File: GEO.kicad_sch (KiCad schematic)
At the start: 17 parts, among them J1 Conn_01x02, U1 Op_Amp

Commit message: changed two pin header
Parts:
- A1: footprint ARDUINO_ARDUINO_MEGA_2560_REV3_A000067 -> footprints:ARDUINO_ARDUINO_MEGA_2560_REV3_A000067; symbol main_pcb:Arduino_Mega -> symbols:Arduino_Mega
- C1: footprint KiCad Footprints:CAPC1608X90 -> footprints:CAPC1608X90; symbol main_pcb:C -> symbols:C
- CO1: footprint JST_B5B-XH-A -> footprints:JST_B5B-XH-A; symbol main_pcb:Conn_CO -> symbols:Conn_CO
- Clk1: footprint TE_5-146280-5 -> footprints:TE_5-146280-5; symbol main_pcb:Clock -> symbols:Clock
- H1, H2: footprint MountingHole:MountingHole_2.1mm -> footprints:MountingHole_2.1mm; symbol main_pcb:MountingHole -> symbols:MountingHole
- J1: footprint Connector_PinHeader_2.00mm:PinHeader_1x02_P2.00mm_Vertical -> Connector_PinSocket_2.54mm:PinSocket_1x02_P2.54mm_Vertical; symbol main_pcb:Conn_01x02 -> symbols:Conn_01x02
- LCD1: footprint CON9_SMT-RA_FCC-FPC2 -> footprints:TE_84952-9_1x09-1MP_P1.0mm_Horizontal; symbol main_pcb:Conn_LCD -> symbols:Conn_LCD
- PM1: footprint KiCad Footprints:JST_SM08B-GHS-TB(LF)(SN) -> footprints:JST_SM08B-GHS-TB(LF)(SN); symbol main_pcb:Conn_PM -> symbols:Conn_PM
- R1, R2: footprint Resistor_THT:R_Axial_DIN0309_L9.0mm_D3.2mm_P12.70mm_Horizontal -> footprints:R_Axial_DIN0309_L9.0mm_D3.2mm_P12.70mm_Horizontal; symbol main_pcb:R -> symbols:R
- R3, R4: footprint KiCad Footprints:R0402 -> footprints:R0402; symbol main_pcb:R -> symbols:R; JLC_3DModel (none) -> 026a4a15ab5c4a92ac0e421d6d013717; JLC_3D_Size (none) -> 1 0.5
- SD1: footprint JST_B6B-XH-A(LF)(SN) -> footprints:JST_B6B-XH-A(LF)(SN); symbol main_pcb:Conn_SD -> symbols:Conn_SD
- TEMP1: footprint KiCad Footprints:JST_B4B-XH-A(LF)(SN) -> footprints:JST_B4B-XH-A(LF)(SN); symbol main_pcb:Conn_Temp -> symbols:Conn_Temp
- U1: footprint Package_TO_SOT_SMD:SOT-353_SC-70-5 -> footprints:SOT-353_SC-70-5; symbol main_pcb:Op_Amp -> symbols:Op_Amp
- U2: footprint KiCad Footprints:DFR1015 Buck_Converter -> footprints:DFR1015 Buck_Converter; symbol main_pcb:Buck_Converter -> symbols:Buck_Converter
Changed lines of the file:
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@@
 	)
 	(symbol
-		(lib_id "main_pcb:Conn_PM")
+		(lib_id "symbols:Conn_PM")
 		(at 139.7 160.02 0)
 		(unit 1)
@@
 			)
 		)
-		(property "Footprint" "KiCad Footprints:JST_SM08B-GHS-TB(LF)(SN)"
+		(property "Footprint" "footprints:JST_SM08B-GHS-TB(LF)(SN)"
 			(at 139.7 160.02 0)
 			(effects
@@
 	)
 	(symbol
-		(lib_id "main_pcb:MountingHole")
+		(lib_id "symbols:MountingHole")
 		(at 241.3 30.48 0)
 		(unit 1)
@@
 			)
 		)
-		(property "Footprint" "MountingHole:MountingHole_2.1mm"
+		(property "Footprint" "footprints:MountingHole_2.1mm"
 			(at 241.3 30.48 0)
 			(effects
@@
 	)
 	(symbol
-		(lib_id "main_pcb:Arduino_Mega")
+		(lib_id "symbols:Arduino_Mega")
 		(at 58.42 111.76 0)
 		(unit 1)
@@
 			)
 		)
-		(property "Footprint" "ARDUINO_ARDUINO_MEGA_2560_REV3_A000067"
+		(property "Footprint" "footprints:ARDUINO_ARDUINO_MEGA_2560_REV3_A000067"
 			(at 58.42 111.76 0)
 			(effects
@@
 	)
 	(symbol
-		(lib_id "main_pcb:R")
+		(lib_id "symbols:R")
 		(at 232.41 68.58 180)
 		(unit 1)
@@
 			)
 		)
-		(property "Footprint" "Resistor_THT:R_Axial_DIN0309_L9.0mm_D3.2mm_P12.70mm_Horizontal"
+		(property "Footprint" "footprints:R_Axial_DIN0309_L9.0mm_D3.2mm_P12.70mm_Horizontal"
 			(at 231.394 68.326 90)
 			(effects
@@
 	)
 	(symbol
-		(lib_id "main_pcb:R")
+		(lib_id "symbols:R")
 		(at 213.36 97.79 180)
 		(unit 1)
@@
 			)
 		)
-		(property "Footprint" "KiCad Footprints:R0402"
+		(property "Footprint" "footprints:R0402"
 			(at 212.344 97.536 90)
 			(effects
@@
 		)
 		(property "Description" "Resistor, US symbol"
+			(at 213.36 97.79 0)
+			(effects
+				(font
+					(size 1.27 1.27)
+				)
+				(hide yes)
+			)
+		)
+		(property "JLC_3DModel" "026a4a15ab5c4a92ac0e421d6d013717"
+			(at 213.36 97.79 0)
+			(effects
+				(font
+					(size 1.27 1.27)
+				)
+				(hide yes)
+			)
+		)
+		(property "JLC_3D_Size" "1 0.5"
 			(at 213.36 97.79 0)
 			(effects
@@
 	)
 	(symbol
-		(lib_id "main_pcb:Conn_01x02")
+		(lib_id "symbols:Conn_01x02")
 		(at 260.35 99.06 270)
 		(unit 1)
@@
 			)
 		)
-		(property "Footprint" "Connector_PinHeader_2.00mm:PinHeader_1x02_P2.00mm_Vertical"
+		(property "Footprint" "Connector_PinSocket_2.54mm:PinSocket_1x02_P2.54mm_Vertical"
 			(at 260.35 99.06 0)
 			(effects
@@
 	)
 	(symbol
-		(lib_id "main_pcb:Conn_CO")
+		(lib_id "symbols:Conn_CO")
 		(at 137.16 119.38 0)
 		(unit 1)
@@
 			)
 		)
-		(property "Footprint" "JST_B5B-XH-A"
+		(property "Footprint" "footprints:JST_B5B-XH-A"
 			(at 137.16 119.38 0)
 			(effects
@@
 	)
 	(symbol
-		(lib_id "main_pcb:MountingHole")
+		(lib_id "symbols:MountingHole")
 		(at 241.3 35.56 0)
 		(unit 1)
@@
 			)
 		)
-		(property "Footprint" "MountingHole:MountingHole_2.1mm"
+		(property "Footprint" "footprints:MountingHole_2.1mm"
 			(at 241.3 35.56 0)
 			(effects
@@
 	)
 	(symbol
-		(lib_id "main_pcb:R")
+		(lib_id "symbols:R")
 		(at 213.36 83.82 180)
 		(unit 1)
@@
 			)
 		)
-		(property "Footprint" "KiCad Footprints:R0402"
+		(property "Footprint" "footprints:R0402"
 			(at 212.344 83.566 90)
 			(effects
@@
 		)
 		(property "Description" "Resistor, US symbol"
+			(at 213.36 83.82 0)
+			(effects
+				(font
+					(size 1.27 1.27)
+				)
+				(hide yes)
+			)
+		)
+		(property "JLC_3DModel" "026a4a15ab5c4a92ac0e421d6d013717"
+			(at 213.36 83.82 0)
+			(effects
+				(font
+					(size 1.27 1.27)
+				)
+				(hide yes)
+			)
+		)
+		(property "JLC_3D_Size" "1 0.5"
 			(at 213.36 83.82 0)
 			(effects
@@
 	)
 	(symbol
-		(lib_id "main_pcb:R")
+		(lib_id "symbols:R")
 		(at 232.41 54.61 180)
 		(unit 1)
@@
 			)
 		)
-		(property "Footprint" "Resistor_THT:R_Axial_DIN0309_L9.0mm_D3.2mm_P12.70mm_Horizontal"
+		(property "Footprint" "footprints:R_Axial_DIN0309_L9.0mm_D3.2mm_P12.70mm_Horizontal"
 			(at 231.394 54.356 90)
 			(effects
@@
 	)
 	(symbol
-		(lib_id "main_pcb:Clock")
+		(lib_id "symbols:Clock")
 		(at 195.58 154.94 0)
 		(unit 1)
@@
 			)
 		)
-		(property "Footprint" "TE_5-146280-5"
+		(property "Footprint" "footprints:TE_5-146280-5"
 			(at 195.58 154.94 0)
 			(effects
@@
 	)
 	(symbol
-		(lib_id "main_pcb:Conn_SD")
+		(lib_id "symbols:Conn_SD")
 		(at 139.7 60.96 0)
 		(unit 1)
@@
 			)
 		)
-		(property "Footprint" "JST_B6B-XH-A(LF)(SN)"
+		(property "Footprint" "footprints:JST_B6B-XH-A(LF)(SN)"
 			(at 139.7 60.96 0)
 			(effects
@@
 	)
 	(symbol
-		(lib_id "main_pcb:Conn_Temp")
+		(lib_id "symbols:Conn_Temp")
 		(at 200.66 129.54 0)
 		(unit 1)
@@
 			)
 		)
-		(property "Footprint" "KiCad Footprints:JST_B4B-XH-A(LF)(SN)"
+		(property "Footprint" "footprints:JST_B4B-XH-A(LF)(SN)"
 			(at 200.66 129.54 0)
 			(effects
@@
 	)
 	(symbol
-		(lib_id "main_pcb:Op_Amp")
+		(lib_id "symbols:Op_Amp")
 		(at 237.49 93.98 0)
 		(unit 1)
@@
 			)
 		)
-		(property "Footprint" "Package_TO_SOT_SMD:SOT-353_SC-70-5"
+		(property "Footprint" "footprints:SOT-353_SC-70-5"
 			(at 242.57 93.98 0)
 			(effects
@@
 	)
 	(symbol
-		(lib_id "main_pcb:Buck_Converter")
+		(lib_id "symbols:Buck_Converter")
 		(at 93.98 189.23 0)
 		(unit 1)
@@
 			)
 		)
-		(property "Footprint" "KiCad Footprints:DFR1015 Buck_Converter"
+		(property "Footprint" "footprints:DFR1015 Buck_Converter"
 			(at 93.98 189.23 0)
 			(effects
@@
 	)
 	(symbol
-		(lib_id "main_pcb:C")
+		(lib_id "symbols:C")
 		(at 245.11 82.55 90)
 		(unit 1)
@@
 			)
 		)
-		(property "Footprint" "KiCad Footprints:CAPC1608X90"
+		(property "Footprint" "footprints:CAPC1608X90"
 			(at 248.92 81.5848 0)
 			(effects
@@
 	)
 	(symbol
-		(lib_id "main_pcb:Conn_LCD")
+		(lib_id "symbols:Conn_LCD")
 		(at 179.07 53.34 0)
 		(unit 1)
@@
 			)
 		)
-		(property "Footprint" "CON9_SMT-RA_FCC-FPC2"
+		(property "Footprint" "footprints:TE_84952-9_1x09-1MP_P1.0mm_Horizontal"
 			(at 179.07 53.34 0)
 			(effects

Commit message: flip buck converter and add screw terminal, gen gerber files
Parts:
- removed H1, H2: MountingHole, footprints:MountingHole_2.1mm, symbol symbols:MountingHole
- added J2: Screw_Terminal_01x02, TerminalBlock:TerminalBlock_MaiXu_MX126-5.0-02P_1x02_P5.00mm, symbol Connector:Screw_Terminal_01x02
- J1: footprint Connector_PinSocket_2.54mm:PinSocket_1x02_P2.54mm_Vertical -> footprints:PinSocket_1x02_P2.54mm_Vertical
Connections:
- net 5V: now also U2.1 (5V_out); no longer U2.3 (5V_out)
- net BAT_IN: now also U2.3 (Bat_in), J2.2 (Pin_2); no longer U2.1 (Bat_in)
- net GND: now also J2.1 (Pin_1)

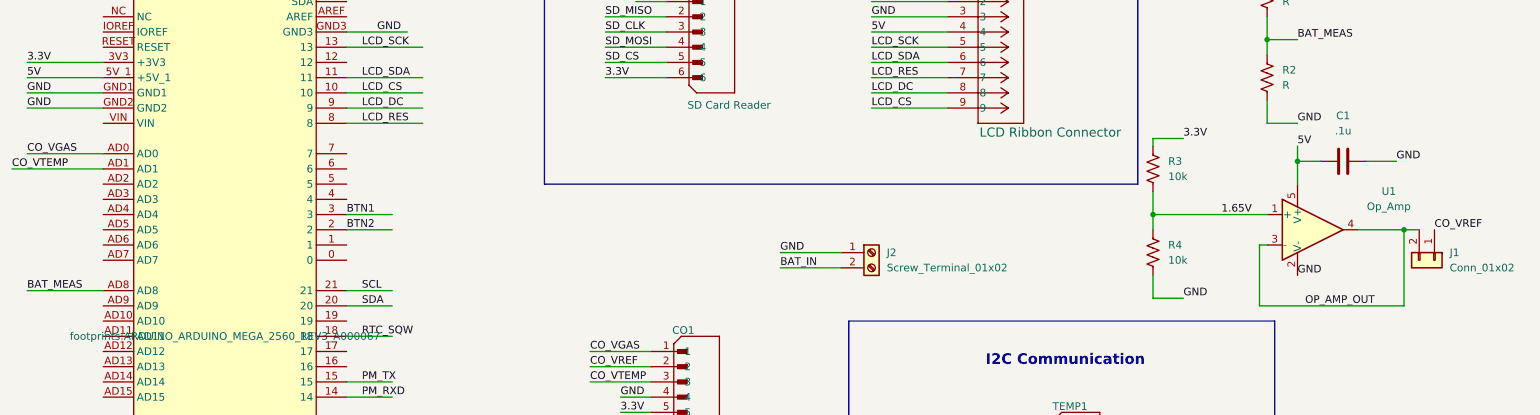
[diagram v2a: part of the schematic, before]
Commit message: removed Vref circuitry from CO sensor and wired Vref to pin A2
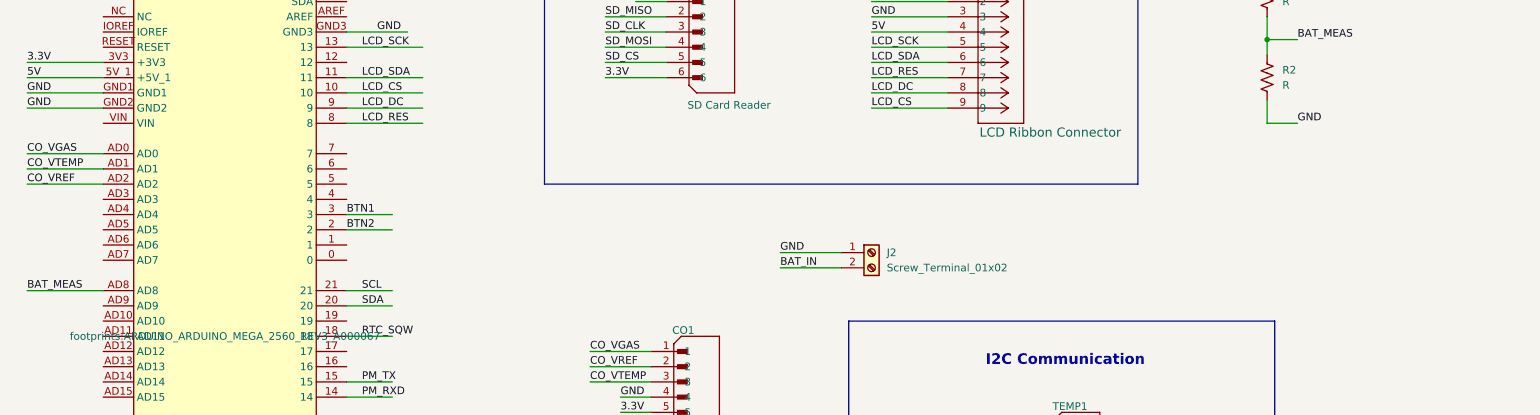
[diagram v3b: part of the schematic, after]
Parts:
- removed C1: .1u, footprints:CAPC1608X90, symbol symbols:C
- removed J1: Conn_01x02, footprints:PinSocket_1x02_P2.54mm_Vertical, symbol symbols:Conn_01x02
- removed R3, R4: 10k, footprints:R0402, symbol symbols:R
- removed U1: Op_Amp, footprints:SOT-353_SC-70-5, symbol symbols:Op_Amp
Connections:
- net CO_VREF: now also A1.AD2

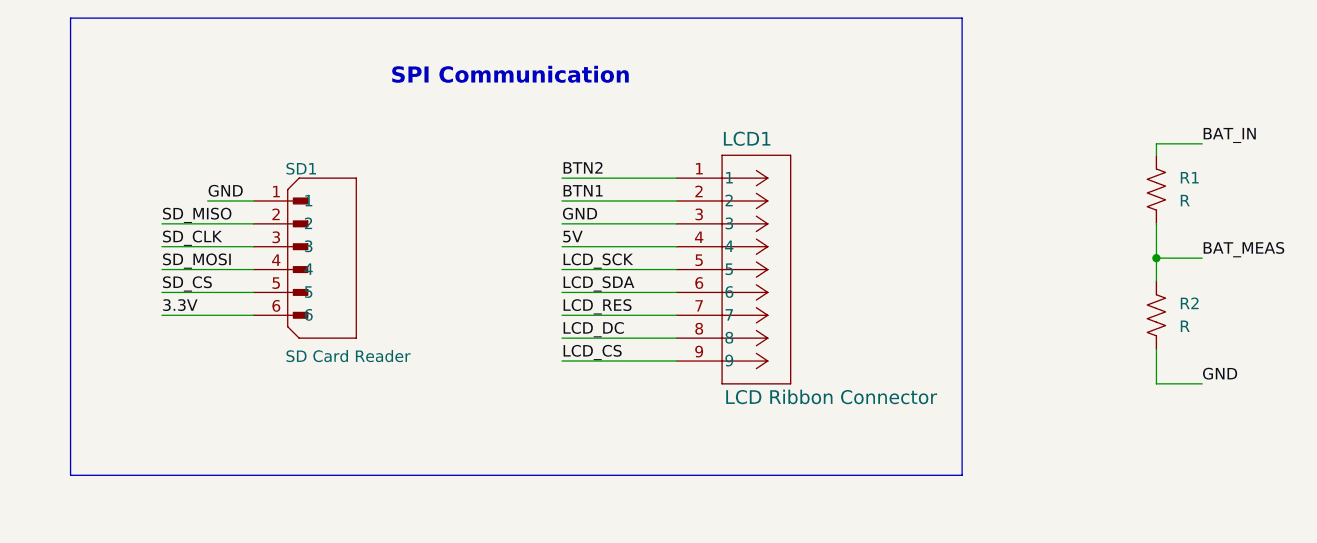
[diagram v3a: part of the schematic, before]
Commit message: gerber 03-24-26, add VRef pin
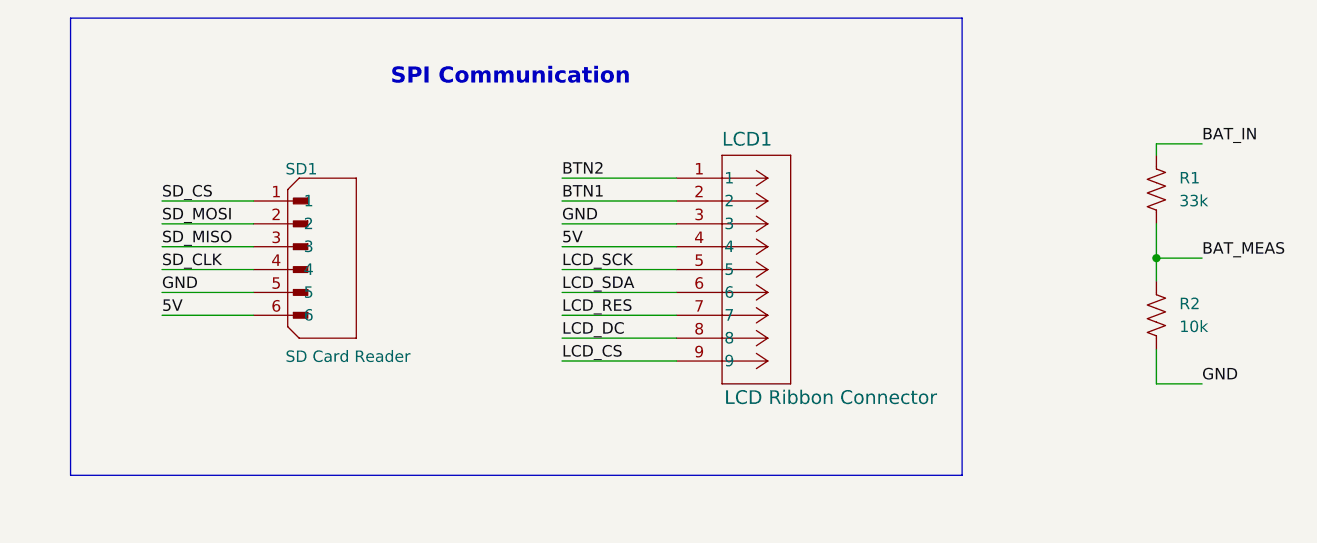
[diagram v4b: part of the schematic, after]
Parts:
- R1: value R -> 33k
- R2: value R -> 10k
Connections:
- net 3.3V: no longer SD1.6
- net 5V: now also SD1.6
- net GND: now also SD1.5; no longer SD1.1
- net SD_CLK: now also SD1.4; no longer SD1.3
- net SD_CS: now also SD1.1; no longer SD1.5
- net SD_MISO: now also SD1.3; no longer SD1.2
- net SD_MOSI: now also SD1.2; no longer SD1.4
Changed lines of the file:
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@@
+	(wire
+		(pts
+			(xy 232.41 49.53) (xy 237.49 49.53)
+		)
+		(stroke
+			(width 0)
+			(type default)
+		)
+	)
+	(wire
+		(pts
+			(xy 78.74 119.38) (xy 86.36 119.38)
+		)
+		(stroke
+			(width 0)
+			(type default)
+		)
+	)
+	(wire
+		(pts
+			(xy 78.74 165.1) (xy 91.44 165.1)
+		)
+		(stroke
+			(width 0)
+			(type default)
+		)
+	)
+	(wire
+		(pts
+			(xy 78.74 73.66) (xy 91.44 73.66)
+		)
+		(stroke
+			(width 0)
+			(type default)
+		)
+	)
+	(wire
+		(pts
+			(xy 119.38 116.84) (xy 129.54 116.84)
+		)
+		(stroke
+			(width 0)
+			(type default)
+		)
+	)
+	(wire
+		(pts
+			(xy 78.74 68.58) (xy 91.44 68.58)
+		)
+		(stroke
+			(width 0)
+			(type default)
+		)
+	)
 	(wire
 		(pts
@@
 	(wire
 		(pts
-			(xy 232.41 49.53) (xy 237.49 49.53)
-		)
-		(stroke
-			(width 0)
-			(type default)
-		)
-	)
-	(wire
-		(pts
-			(xy 78.74 119.38) (xy 86.36 119.38)
-		)
-		(stroke
-			(width 0)
-			(type default)
-		)
-	)
-	(wire
-		(pts
-			(xy 78.74 165.1) (xy 91.44 165.1)
-		)
-		(stroke
-			(width 0)
-			(type default)
-		)
-	)
-	(wire
-		(pts
-			(xy 78.74 73.66) (xy 91.44 73.66)
-		)
-		(stroke
-			(width 0)
-			(type default)
-		)
-	)
-	(wire
-		(pts
-			(xy 119.38 116.84) (xy 129.54 116.84)
-		)
-		(stroke
-			(width 0)
-			(type default)
-		)
-	)
-	(wire
-		(pts
-			(xy 78.74 68.58) (xy 91.44 68.58)
-		)
-		(stroke
-			(width 0)
-			(type default)
-		)
-	)
-	(wire
-		(pts
 			(xy 38.1 165.1) (xy 25.4 165.1)
 		)
@@
 	(wire
 		(pts
+			(xy 121.92 66.04) (xy 132.08 66.04)
+		)
+		(stroke
+			(width 0)
+			(type default)
+		)
+	)
+	(wire
+		(pts
 			(xy 78.74 71.12) (xy 91.44 71.12)
 		)
@@
 	(wire
 		(pts
+			(xy 121.92 58.42) (xy 132.08 58.42)
+		)
+		(stroke
+			(width 0)
+			(type default)
+		)
+	)
+	(wire
+		(pts
 			(xy 78.74 111.76) (xy 86.36 111.76)
 		)
@@
 	(wire
 		(pts
+			(xy 121.92 60.96) (xy 132.08 60.96)
+		)
+		(stroke
+			(width 0)
+			(type default)
+		)
+	)
+	(wire
+		(pts
 			(xy 78.74 93.98) (xy 86.36 93.98)
 		)
@@
 	(wire
 		(pts
+			(xy 121.92 55.88) (xy 132.08 55.88)
+		)
+		(stroke
+			(width 0)
+			(type default)
+		)
+	)
+	(wire
+		(pts
 			(xy 166.37 66.04) (xy 179.07 66.04)
 		)
@@
 	(wire
 		(pts
-			(xy 121.92 66.04) (xy 132.08 66.04)
-		)
-		(stroke
-			(width 0)
-			(type default)
-		)
-	)
-	(wire
-		(pts
 			(xy 232.41 62.23) (xy 237.49 62.23)
 		)
@@
 	(wire
 		(pts
-			(xy 127 55.88) (xy 132.08 55.88)
-		)
-		(stroke
-			(width 0)
-			(type default)
-		)
-	)
-	(wire
-		(pts
 			(xy 78.74 167.64) (xy 91.44 167.64)
 		)
@@
 		(pts
 			(xy 78.74 121.92) (xy 86.36 121.92)
-		)
-		(stroke
-			(width 0)
-			(type default)
-		)
-	)
-	(wire
-		(pts
-			(xy 121.92 58.42) (xy 132.08 58.42)
-		)
-		(stroke
-			(width 0)
-			(type default)
-		)
-	)
-	(wire
-		(pts
-			(xy 121.92 60.96) (xy 132.08 60.96)
 		)
 		(stroke
@@
 	)
 	(label "SD_CS"
-		(at 121.92 66.04 0)
+		(at 121.92 55.88 0)
 		(effects
 			(font
@@
 	)
 	(label "SD_MISO"
-		(at 121.92 58.42 0)
+		(at 121.92 60.96 0)
 		(effects
 			(font
@@
 		)
 	)
-	(label "3.3V"
+	(label "5V"
 		(at 121.92 68.58 0)
 		(effects
@@
 	)
 	(label "SD_MOSI"
-		(at 121.92 63.5 0)
+		(at 121.92 58.42 0)
 		(effects
 			(font
@@
 	)
 	(label "SD_CLK"
-		(at 121.92 60.96 0)
+		(at 121.92 63.5 0)
 		(effects
 			(font
@@
 	)
 	(label "GND"
-		(at 127 55.88 0)
+		(at 121.92 66.04 0)
 		(effects
 			(font
@@
 			)
 		)
-		(property "Value" "R"
+		(property "Value" "10k"
 			(at 234.95 69.8499 0)
 			(effects
@@
 			)
 		)
-		(property "Value" "R"
+		(property "Value" "33k"
 			(at 234.95 55.8799 0)
 			(effects
